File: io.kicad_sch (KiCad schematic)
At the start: 39 parts, among them J10 RIGHT WHEEL SENS, J11 STARTER CON, J12 USB_C_Receptacle, J13 USB_C_Receptacle, J14 CAN, J15 3.3V OUT, J16 5V OUT, J17 7.5V OUT, J18 OIL CON, J19 IAT CON, J20 PRIM TRIGG CON, J21 SEC TRIGG CON, J22 EGT CON, J23 DATA LOGGER CON, J24 IGN CON, J25 INJ CON, J26 MAP, J27 CLT CON, J28 TPS CON, J3 EMU_BLACK_A, J4 EMU_BLACK_B, J6 INJ_&_STARTER, J7 16V OUT, J8 SERVO, J9 LEFT WHEEL SENS, K1 FINDER-34.51 INJ, K2 FINDER-34.51 STARTER, K3 FINDER-34.51 INJ, Q2 IRFP1405PBF, Q3 IRFP1405PBF, Q4 IRFP1405PBF, U7 TXS0108EPWR

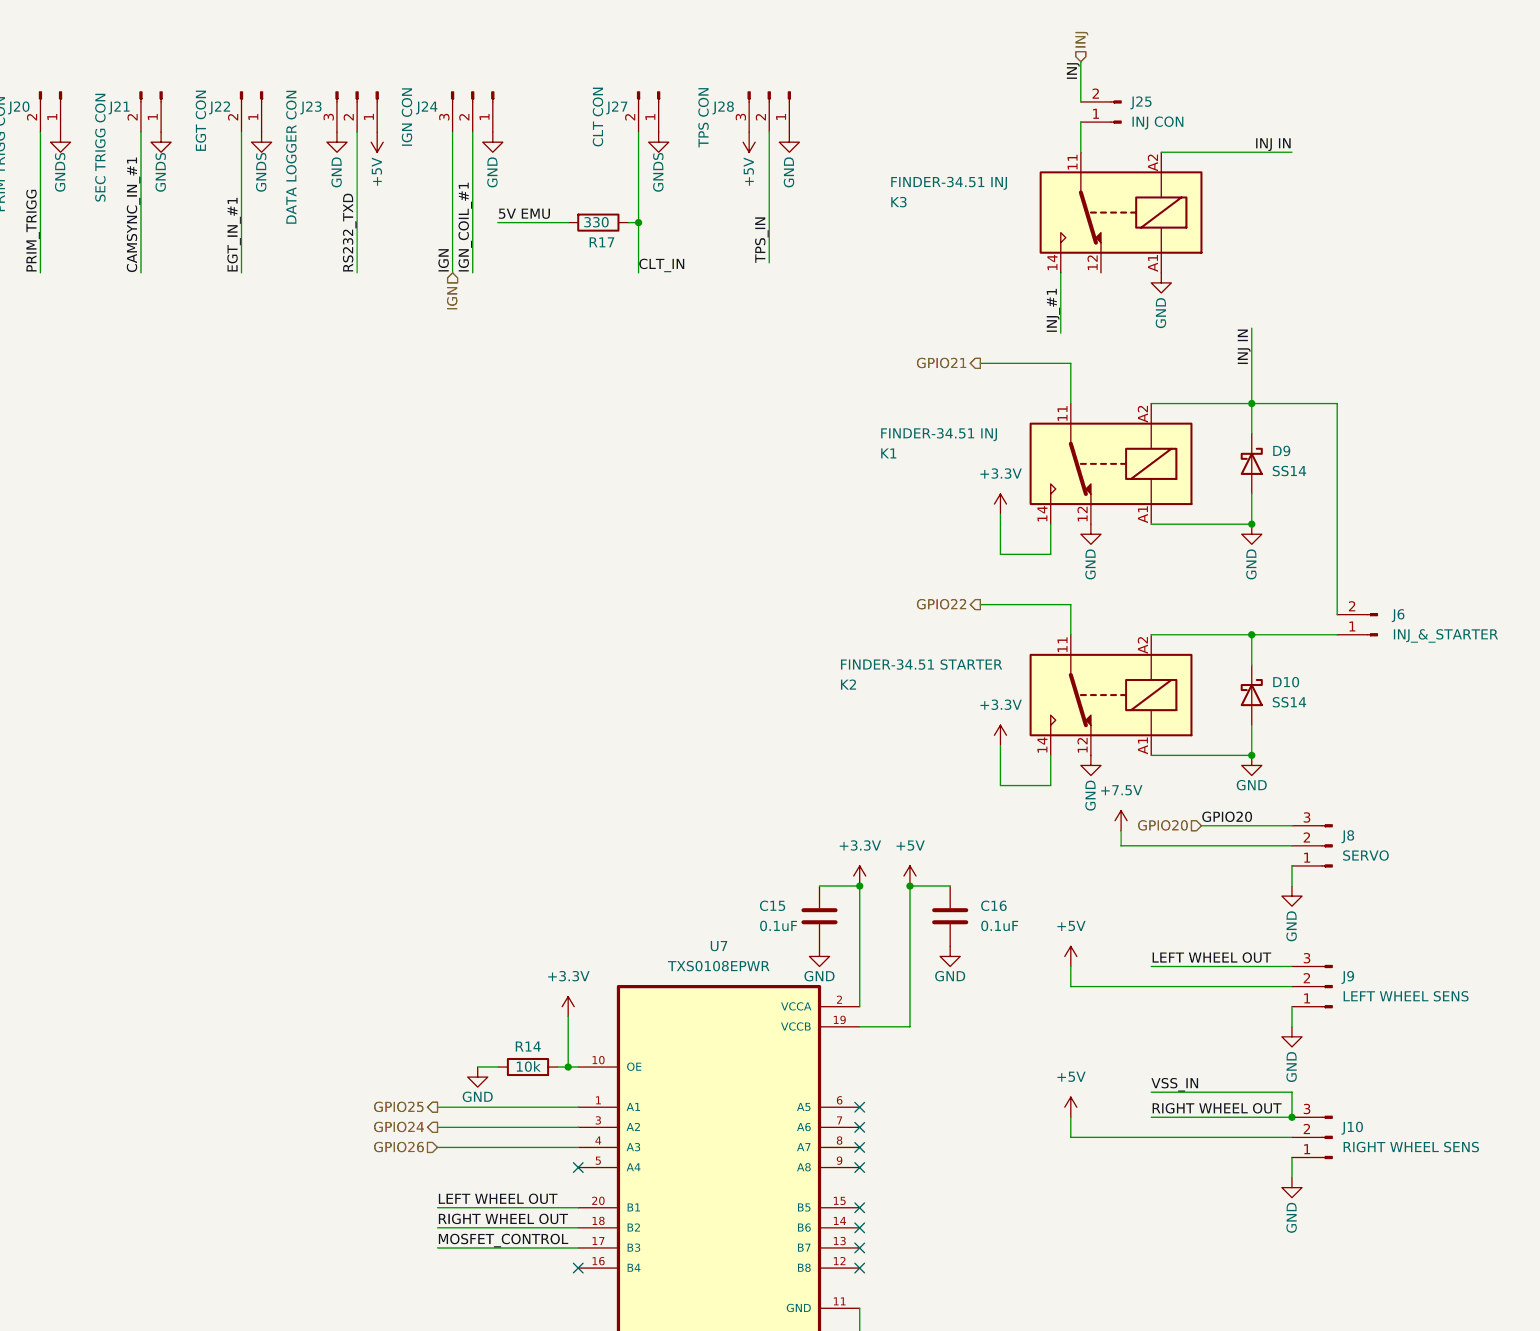
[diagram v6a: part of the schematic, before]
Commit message: Added lambda connection, switching between PWM and 3.3v signal to drive mosfets.
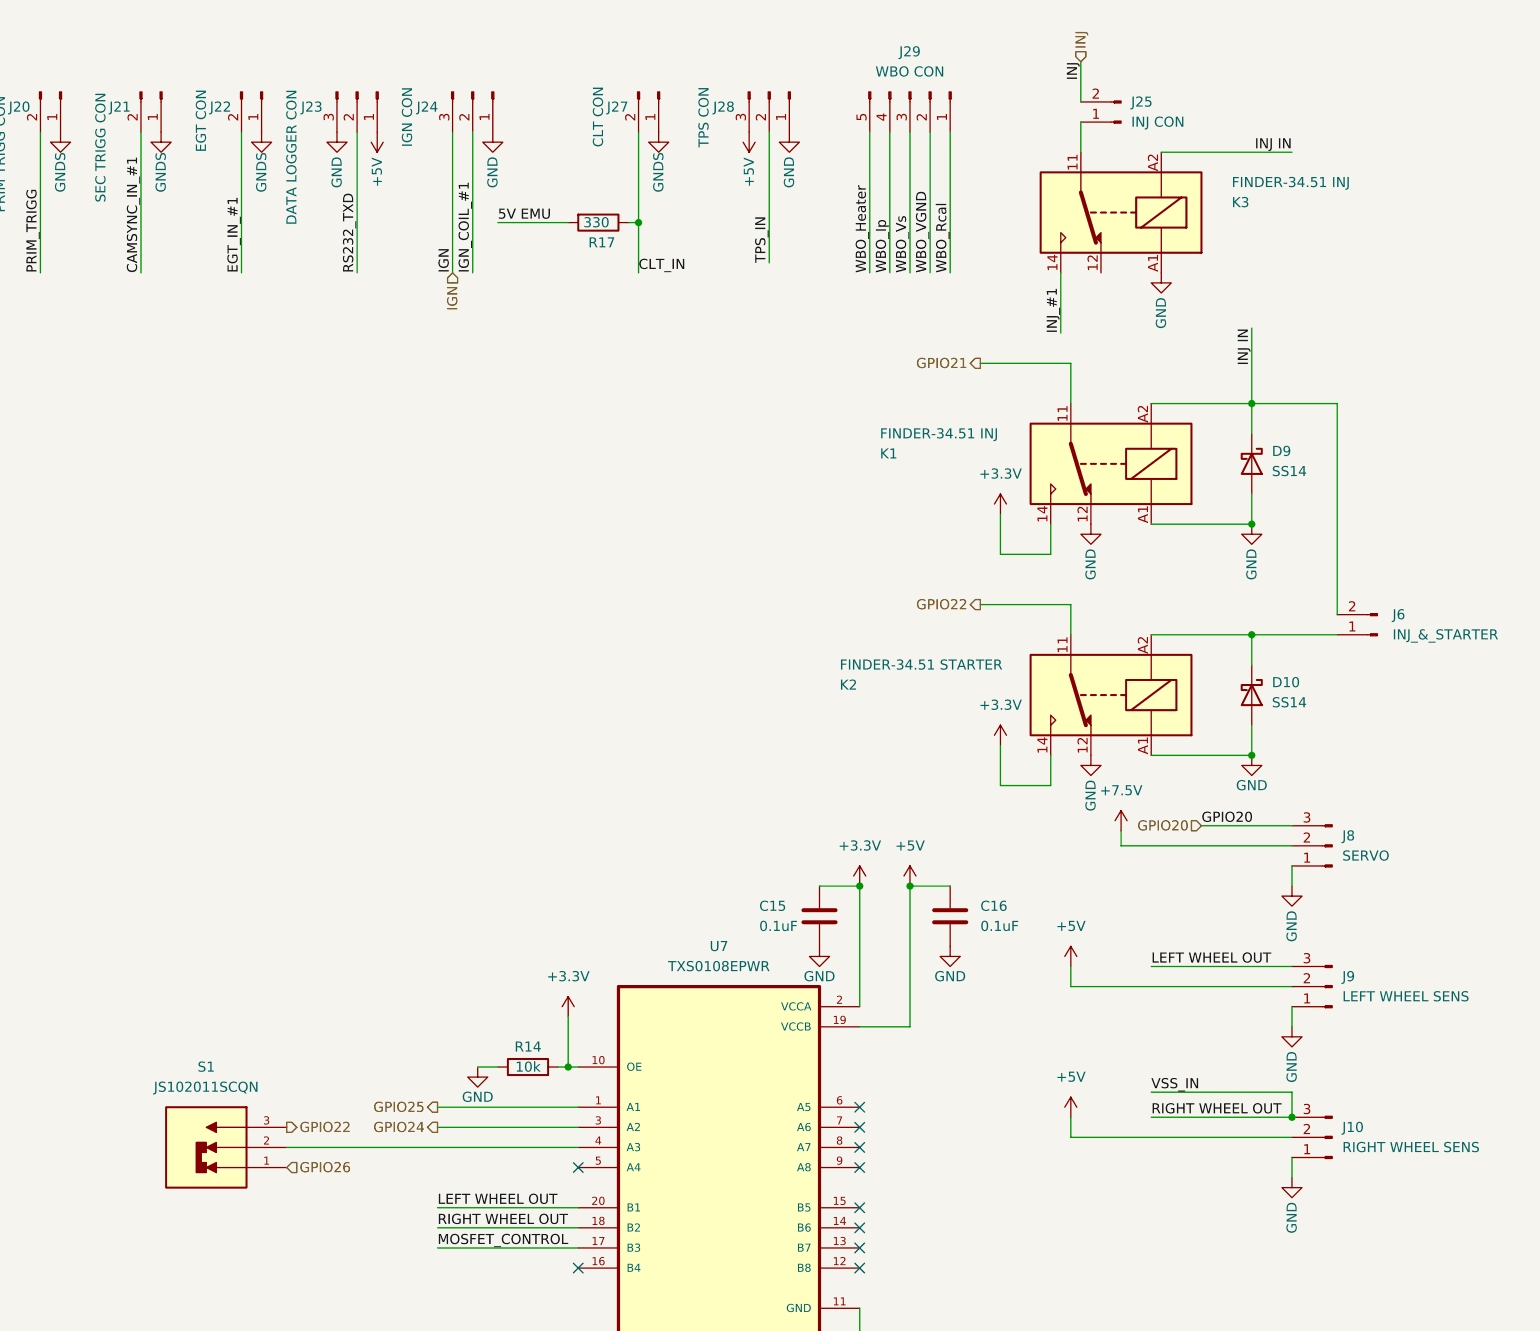
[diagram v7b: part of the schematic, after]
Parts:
- added J29: WBO CON, TerminalBlock_Phoenix:TerminalBlock_Phoenix_MPT-0,5-5-2.54_1x05_P2.54mm_Horizontal, symbol Connector:Conn_01x05_Male
- added S1: JS102011SCQN, lib:SW_JS102011SCQN, symbol JS102011SCQN:JS102011SCQN
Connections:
- net GPIO22: now also S1.3
- net GPIO26: now also S1.1; no longer U7.4 (A3)
- net WBO_Heater: now also J29.5 (Pin_5)
- net WBO_Ip: now also J29.4 (Pin_4)
- net WBO_Rcal: now also J29.1 (Pin_1)
- net WBO_VGND: now also J29.2 (Pin_2)
- net WBO_Vs: now also J29.3 (Pin_3)
- new net: S1.2, U7.4 (A3)
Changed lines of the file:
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@@
+    (stroke (width 0) (type default) (color 0 0 0 0))
+  )
+  (wire (pts (xy 327.66 43.18) (xy 327.66 25.4))
+    (stroke (width 0) (type default) (color 0 0 0 0))
+  )
+  (wire (pts (xy 330.2 43.18) (xy 330.2 25.4))
     (stroke (width 0) (type default) (color 0 0 0 0))
   )
@@
     (stroke (width 0) (type default) (color 0 0 0 0))
   )
+  (wire (pts (xy 332.74 43.18) (xy 332.74 25.4))
+    (stroke (width 0) (type default) (color 0 0 0 0))
+  )
   (wire (pts (xy 273.05 148.59) (xy 290.83 148.59))
     (stroke (width 0) (type default) (color 0 0 0 0))
@@
     (stroke (width 0) (type default) (color 0 0 0 0))
   )
+  (wire (pts (xy 335.28 43.18) (xy 335.28 25.4))
+    (stroke (width 0) (type default) (color 0 0 0 0))
+  )
   (wire (pts (xy 353.06 85.09) (xy 353.06 88.9))
     (stroke (width 0) (type default) (color 0 0 0 0))
@@
     (stroke (width 0) (type default) (color 0 0 0 0))
   )
-  (wire (pts (xy 273.05 153.67) (xy 290.83 153.67))
-    (stroke (width 0) (type default) (color 0 0 0 0))
-  )
   (wire (pts (xy 110.49 20.32) (xy 110.49 38.1))
     (stroke (width 0) (type default) (color 0 0 0 0))
@@
     (stroke (width 0) (type default) (color 0 0 0 0))
   )
+  (wire (pts (xy 337.82 43.18) (xy 337.82 25.4))
+    (stroke (width 0) (type default) (color 0 0 0 0))
+  )
   (wire (pts (xy 340.36 215.9) (xy 359.41 215.9))
     (stroke (width 0) (type default) (color 0 0 0 0))
@@
     (stroke (width 0) (type default) (color 0 0 0 0))
   )
+  (wire (pts (xy 254 153.67) (xy 290.83 153.67))
+    (stroke (width 0) (type default) (color 0 0 0 0))
+  )
   (wire (pts (xy 375.92 59.69) (xy 375.92 63.5))
     (stroke (width 0) (type default) (color 0 0 0 0))
@@
     (effects (font (size 1.27 1.27)) (justify left bottom))
   )
+  (label "WBO_Heater" (at 327.66 43.18 90)
+    (effects (font (size 1.27 1.27)) (justify left bottom))
+  )
   (label "USB_PASSTHROUH_VSYS" (at 71.12 172.72 180)
     (effects (font (size 1.27 1.27)) (justify right bottom))
@@
     (effects (font (size 1.27 1.27)) (justify left bottom))
   )
+  (label "WBO_Rcal" (at 337.82 43.18 90)
+    (effects (font (size 1.27 1.27)) (justify left bottom))
+  )
   (label "INJ_#4" (at 97.79 20.32 270)
     (effects (font (size 1.27 1.27)) (justify right bottom))
@@
     (effects (font (size 1.27 1.27)) (justify left bottom))
   )
+  (label "WBO_VGND" (at 335.28 43.18 90)
+    (effects (font (size 1.27 1.27)) (justify left bottom))
+  )
   (label "USB_PASSTHROUH_DP" (at 71.12 193.04 180)
     (effects (font (size 1.27 1.27)) (justify right bottom))
@@
     (effects (font (size 1.27 1.27)) (justify left bottom))
   )
+  (label "WBO_Vs" (at 332.74 43.18 90)
+    (effects (font (size 1.27 1.27)) (justify left bottom))
+  )
   (label "5V EMU" (at 178.435 36.83 0)
     (effects (font (size 1.27 1.27)) (justify left bottom))
@@
   )
   (label "GPIO20" (at 369.57 113.03 0)
+    (effects (font (size 1.27 1.27)) (justify left bottom))
+  )
+  (label "WBO_Ip" (at 330.2 43.18 90)
     (effects (font (size 1.27 1.27)) (justify left bottom))
   )
@@
     )
   )
+  (hierarchical_label "GPIO26" (shape input) (at 254 156.21 0)
+    (effects (font (size 1.27 1.27)) (justify left))
+  )
   (hierarchical_label "EMU" (shape input) (at 52.07 68.58 270)
     (effects (font (size 1.27 1.27)) (justify right))
@@
     (effects (font (size 1.27 1.27)) (justify right))
   )
+  (hierarchical_label "GPIO22" (shape output) (at 254 151.13 0)
+    (effects (font (size 1.27 1.27)) (justify left))
+  )
   (hierarchical_label "STARTER" (shape input) (at 367.03 181.61 180)
     (effects (font (size 1.27 1.27)) (justify right))
@@
   )
   (hierarchical_label "GPIO20" (shape input) (at 369.57 113.03 180)
-    (effects (font (size 1.27 1.27)) (justify right))
-  )
-  (hierarchical_label "GPIO26" (shape input) (at 273.05 153.67 180)
     (effects (font (size 1.27 1.27)) (justify right))
   )
@@
     (pin "1")
   )
+  (symbol (lib_id "Connector:Conn_01x05_Male") (at 332.74 20.32 270) (unit 1)
+    (in_bom yes) (on_board yes)
+    (property "Reference" "J29" (id 0) (at 332.74 15.24 90))
+    (property "Value" "WBO CON" (id 1) (at 332.74 17.78 90))
+    (property "Footprint" "TerminalBlock_Phoenix:TerminalBlock_Phoenix_MPT-0,5-5-2.54_1x05_P2.54mm_Horizontal" (id 2) (at 332.74 20.32 0)
+      (effects (font (size 1.27 1.27)) hide)
+    )
+    (property "Datasheet" "~" (id 3) (at 332.74 20.32 0)
+      (effects (font (size 1.27 1.27)) hide)
+    )
+    (pin "1")
+    (pin "2")
+    (pin "3")
+    (pin "4")
+    (pin "5")
+  )
   (symbol (lib_id "Connector:Conn_01x02_Male") (at 238.125 20.32 270) (unit 1)
     (in_bom yes) (on_board yes)
@@
     )
     (pin "1")
+  )
+  (symbol (lib_id "JS102011SCQN:JS102011SCQN") (at 243.84 153.67 180) (unit 1)
+    (in_bom yes) (on_board yes) (fields_autoplaced)
+    (property "Reference" "S1" (id 0) (at 243.84 143.51 0))
+    (property "Value" "JS102011SCQN" (id 1) (at 243.84 146.05 0))
+    (property "Footprint" "lib:SW_JS102011SCQN" (id 2) (at 243.84 153.67 0)
+      (effects (font (size 1.27 1.27)) (justify bottom) hide)
+    )
+    (property "Datasheet" "" (id 3) (at 243.84 153.67 0)
+      (effects (font (size 1.27 1.27)) hide)
+    )
+    (property "PARTREV" "8 Oct 21" (id 4) (at 243.84 153.67 0)
+      (effects (font (size 1.27 1.27)) (justify bottom) hide)
+    )
+    (property "STANDARD" "Manufacturer Recommendations" (id 5) (at 243.84 153.67 0)
+      (effects (font (size 1.27 1.27)) (justify bottom) hide)
+    )
+    (property "MAXIMUM_PACKAGE_HEIGHT" "5.5mm" (id 6) (at 243.84 153.67 0)
+      (effects (font (size 1.27 1.27)) (justify bottom) hide)
+    )
+    (property "MANUFACTURER" "C&K" (id 7) (at 243.84 153.67 0)
+      (effects (font (size 1.27 1.27)) (justify bottom) hide)
+    )
+    (pin "1")
+    (pin "2")
+    (pin "3")
   )
   (symbol (lib_id "Connector:Conn_01x02_Male") (at 250.825 20.32 270) (unit 1)
@@
   (symbol (lib_id "Relay:FINDER-34.51") (at 359.41 35.56 180) (unit 1)
     (in_bom yes) (on_board yes)
-    (property "Reference" "K3" (id 0) (at 330.2 34.29 0)
-      (effects (font (size 1.27 1.27)) (justify right))
-    )
-    (property "Value" "FINDER-34.51 INJ" (id 1) (at 330.2 31.75 0)
-      (effects (font (size 1.27 1.27)) (justify right))
-    )
+    (property "Reference" "K3" (id 0) (at 373.38 34.29 0)
+      (effects (font (size 1.27 1.27)) (justify right))
+    )
+    (property "Value" "FINDER-34.51 INJ" (id 1) (at 373.38 31.75 0)
+      (effects (font (size 1.27 1.27)) (justify right))
+    )

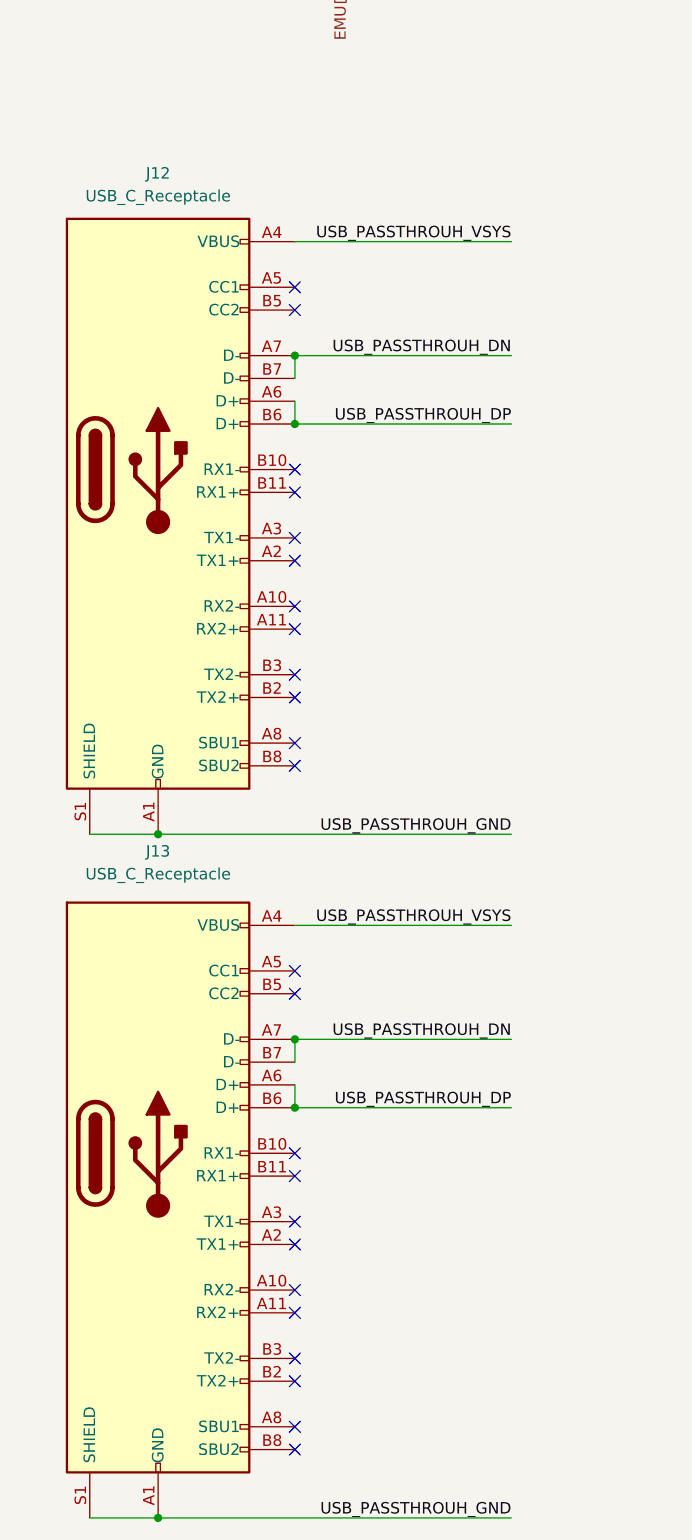
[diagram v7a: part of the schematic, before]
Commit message: Added DS1307 RTC and micro SD card
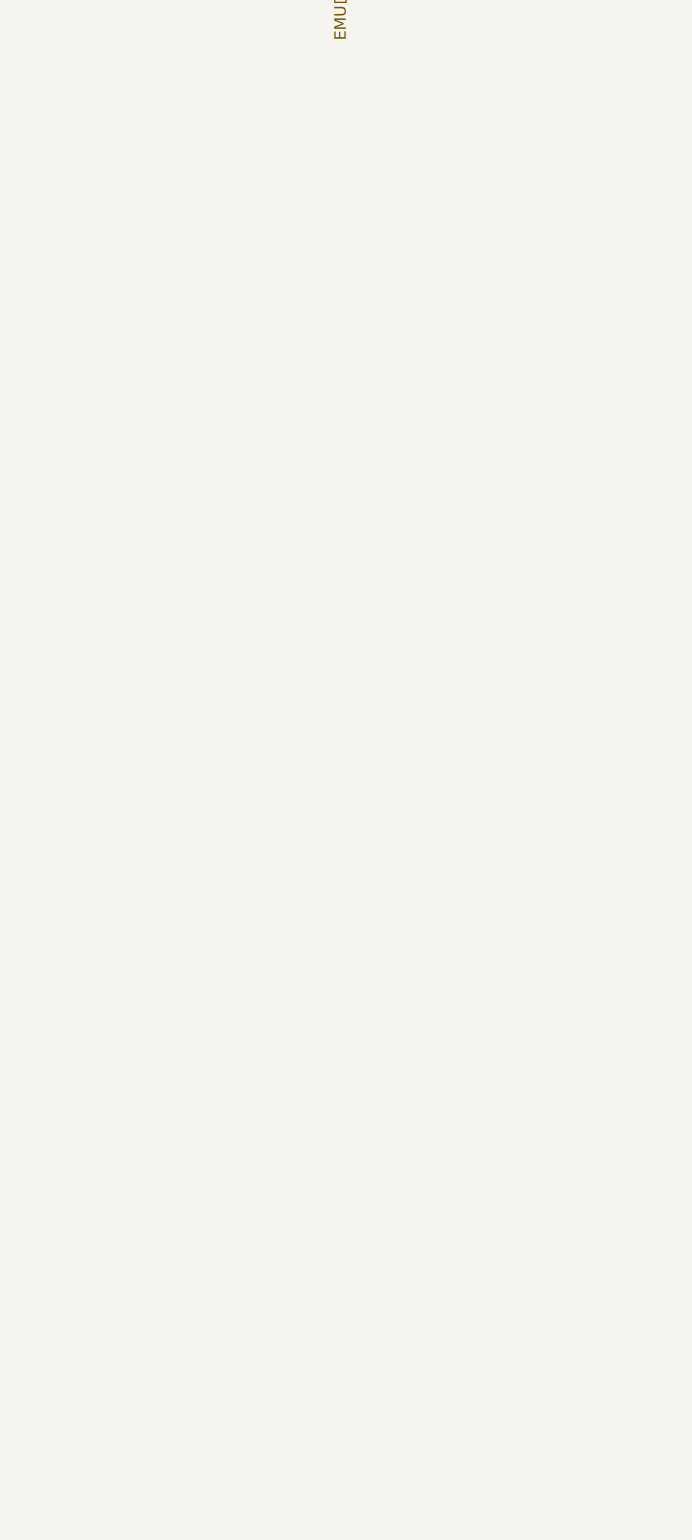
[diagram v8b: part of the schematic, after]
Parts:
- removed J12, J13: USB_C_Receptacle, Connector_USB:USB_C_Receptacle_HRO_TYPE-C-31-M-12, symbol Connector:USB_C_Receptacle
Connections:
- no-connect marks 36 -> 12
